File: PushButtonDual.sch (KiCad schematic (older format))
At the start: 3 parts, among them SW3 PCB_Push_Button, SW4 PCB_Push_Button

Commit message: Place the main components on the PCB
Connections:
- net +3V3: now also SW3.1; no longer SW3.2
- net Button: now also SW3.2; no longer SW3.1
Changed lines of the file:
@@
 AR Path="/603E03AA/604DE92D/604E1842" Ref="R21"  Part="1"
 AR Path="/603E03AA/604E2A9A/604E1842" Ref="R25"  Part="1"
-F 0 "R25" H 5070 4046 50  0000 L CNN
+F 0 "R21" H 5070 4046 50  0000 L CNN
 F 1 "10k" H 5070 3955 50  0000 L CNN
 F 2 "Resistor_SMD:R_0603_1608Metric" V 4930 4000 50  0001 C CNN
@@
 Text HLabel 6000 3500 2    50   Output ~ 0
 Button
-$Comp
-L Switch:SW_Push SW?
-U 1 1 604E42E5
-P 4750 3000
-AR Path="/603E03AA/603C09F0/604E42E5" Ref="SW?"  Part="1"
-AR Path="/603E03AA/603C05C6/604E42E5" Ref="SW?"  Part="1"
-AR Path="/603E03AA/603C0699/604E42E5" Ref="SW?"  Part="1"
-AR Path="/603E03AA/603C06CF/604E42E5" Ref="SW?"  Part="1"
-AR Path="/603E03AA/604DE92D/604E42E5" Ref="SW3"  Part="1"
-AR Path="/603E03AA/604E2A9A/604E42E5" Ref="SW5"  Part="1"
-F 0 "SW5" V 4800 3200 50  0000 L CNN
-F 1 "PCB_Push_Button" V 4700 3200 50  0000 L CNN
-F 2 "LitterRobot:PCB_Push_Button_5mm_0.4mm" H 4750 3200 50  0001 C CNN
-F 3 "~" H 4750 3200 50  0001 C CNN
-	1    4750 3000
-	0    -1   -1   0
-$EndComp
 Wire Wire Line
 	4750 2800 5000 2800
@@
 AR Path="/603E03AA/604DE92D/604E185B" Ref="SW4"  Part="1"
 AR Path="/603E03AA/604E2A9A/604E185B" Ref="SW6"  Part="1"
-F 0 "SW6" V 5200 3200 50  0000 L CNN
+F 0 "SW4" V 5200 3200 50  0000 L CNN
 F 1 "PCB_Push_Button" V 5300 3200 50  0000 L CNN
 F 2 "LitterRobot:PCB_Push_Button_5mm_0.4mm" H 5250 3200 50  0001 C CNN
@@
 	0    1    1    0
 $EndComp
+$Comp
+L Switch:SW_Push SW?
+U 1 1 604E42E5
+P 4750 3000
+AR Path="/603E03AA/603C09F0/604E42E5" Ref="SW?"  Part="1"
+AR Path="/603E03AA/603C05C6/604E42E5" Ref="SW?"  Part="1"
+AR Path="/603E03AA/603C0699/604E42E5" Ref="SW?"  Part="1"
+AR Path="/603E03AA/603C06CF/604E42E5" Ref="SW?"  Part="1"
+AR Path="/603E03AA/604DE92D/604E42E5" Ref="SW3"  Part="1"
+AR Path="/603E03AA/604E2A9A/604E42E5" Ref="SW5"  Part="1"
+F 0 "SW3" V 4700 3200 50  0000 L CNN
+F 1 "PCB_Push_Button" V 4800 3200 50  0000 L CNN
+F 2 "LitterRobot:PCB_Push_Button_5mm_0.4mm" H 4750 3200 50  0001 C CNN
+F 3 "~" H 4750 3200 50  0001 C CNN
+	1    4750 3000
+	0    -1   1    0
+$EndComp
 $EndSCHEMATC

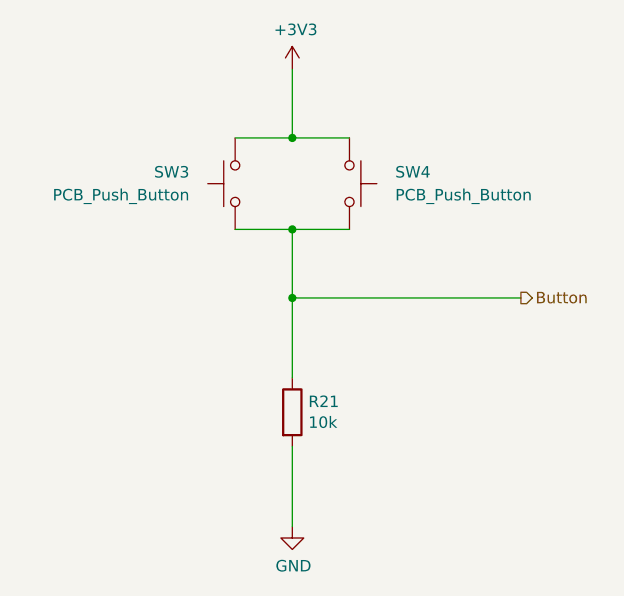
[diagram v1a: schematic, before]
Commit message: Add fuse and more inter-page signals
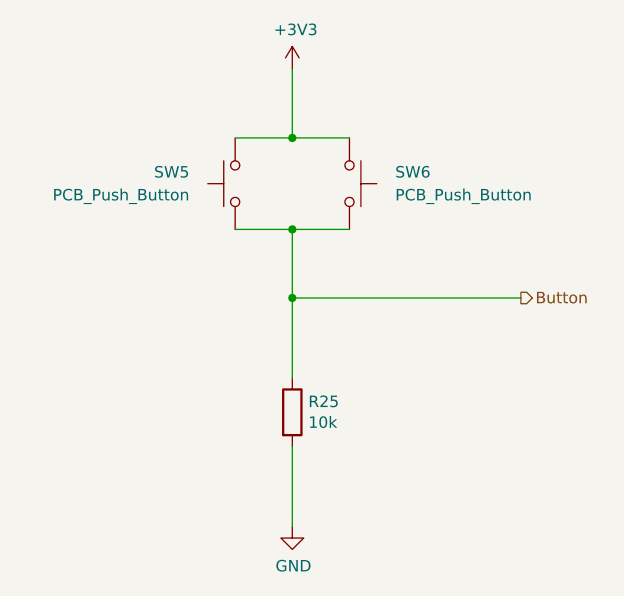
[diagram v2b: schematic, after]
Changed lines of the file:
@@
 AR Path="/603E03AA/604DE92D/604E1842" Ref="R21"  Part="1"
 AR Path="/603E03AA/604E2A9A/604E1842" Ref="R25"  Part="1"
-F 0 "R21" H 5070 4046 50  0000 L CNN
+AR Path="/603F1F4D/605BE155/604E1842" Ref="R?"  Part="1"
+AR Path="/603F1F4D/605BE15D/604E1842" Ref="R?"  Part="1"
+F 0 "R25" H 5070 4046 50  0000 L CNN
 F 1 "10k" H 5070 3955 50  0000 L CNN
 F 2 "Resistor_SMD:R_0603_1608Metric" V 4930 4000 50  0001 C CNN
@@
 AR Path="/603E03AA/603C06CF/604E1848" Ref="#PWR?"  Part="1"
 AR Path="/603E03AA/603C09F0/604E1848" Ref="#PWR?"  Part="1"
-AR Path="/603E03AA/604DE92D/604E1848" Ref="#PWR037"  Part="1"
-AR Path="/603E03AA/604E2A9A/604E1848" Ref="#PWR043"  Part="1"
-F 0 "#PWR043" H 5000 2350 50  0001 C CNN
+AR Path="/603E03AA/604DE92D/604E1848" Ref="#PWR040"  Part="1"
+AR Path="/603E03AA/604E2A9A/604E1848" Ref="#PWR046"  Part="1"
+AR Path="/603F1F4D/605BE155/604E1848" Ref="#PWR?"  Part="1"
+AR Path="/603F1F4D/605BE15D/604E1848" Ref="#PWR?"  Part="1"
+F 0 "#PWR046" H 5000 2350 50  0001 C CNN
 F 1 "+3V3" H 5015 2673 50  0000 C CNN
 F 2 "" H 5000 2500 50  0001 C CNN
@@
 AR Path="/603E03AA/603C06CF/604E184E" Ref="#PWR?"  Part="1"
 AR Path="/603E03AA/603C09F0/604E184E" Ref="#PWR?"  Part="1"
-AR Path="/603E03AA/604DE92D/604E184E" Ref="#PWR038"  Part="1"
-AR Path="/603E03AA/604E2A9A/604E184E" Ref="#PWR044"  Part="1"
-F 0 "#PWR044" H 5000 4250 50  0001 C CNN
+AR Path="/603E03AA/604DE92D/604E184E" Ref="#PWR041"  Part="1"
+AR Path="/603E03AA/604E2A9A/604E184E" Ref="#PWR047"  Part="1"
+AR Path="/603F1F4D/605BE155/604E184E" Ref="#PWR?"  Part="1"
+AR Path="/603F1F4D/605BE15D/604E184E" Ref="#PWR?"  Part="1"
+F 0 "#PWR047" H 5000 4250 50  0001 C CNN
 F 1 "GND" H 5005 4327 50  0000 C CNN
 F 2 "" H 5000 4500 50  0001 C CNN
@@
 AR Path="/603E03AA/604DE92D/604E185B" Ref="SW4"  Part="1"
 AR Path="/603E03AA/604E2A9A/604E185B" Ref="SW6"  Part="1"
-F 0 "SW4" V 5200 3200 50  0000 L CNN
+AR Path="/603F1F4D/605BE155/604E185B" Ref="SW?"  Part="1"
+AR Path="/603F1F4D/605BE15D/604E185B" Ref="SW?"  Part="1"
+F 0 "SW6" V 5200 3200 50  0000 L CNN
 F 1 "PCB_Push_Button" V 5300 3200 50  0000 L CNN
 F 2 "LitterRobot:PCB_Push_Button_5mm_0.4mm" H 5250 3200 50  0001 C CNN
@@
 AR Path="/603E03AA/604DE92D/604E42E5" Ref="SW3"  Part="1"
 AR Path="/603E03AA/604E2A9A/604E42E5" Ref="SW5"  Part="1"
-F 0 "SW3" V 4700 3200 50  0000 L CNN
+AR Path="/603F1F4D/605BE155/604E42E5" Ref="SW?"  Part="1"
+AR Path="/603F1F4D/605BE15D/604E42E5" Ref="SW?"  Part="1"
+F 0 "SW5" V 4700 3200 50  0000 L CNN
 F 1 "PCB_Push_Button" V 4800 3200 50  0000 L CNN
 F 2 "LitterRobot:PCB_Push_Button_5mm_0.4mm" H 4750 3200 50  0001 C CNN
